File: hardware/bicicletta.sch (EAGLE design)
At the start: 21 parts, among them IC1 LM5017, IC2 LM1117-3.3

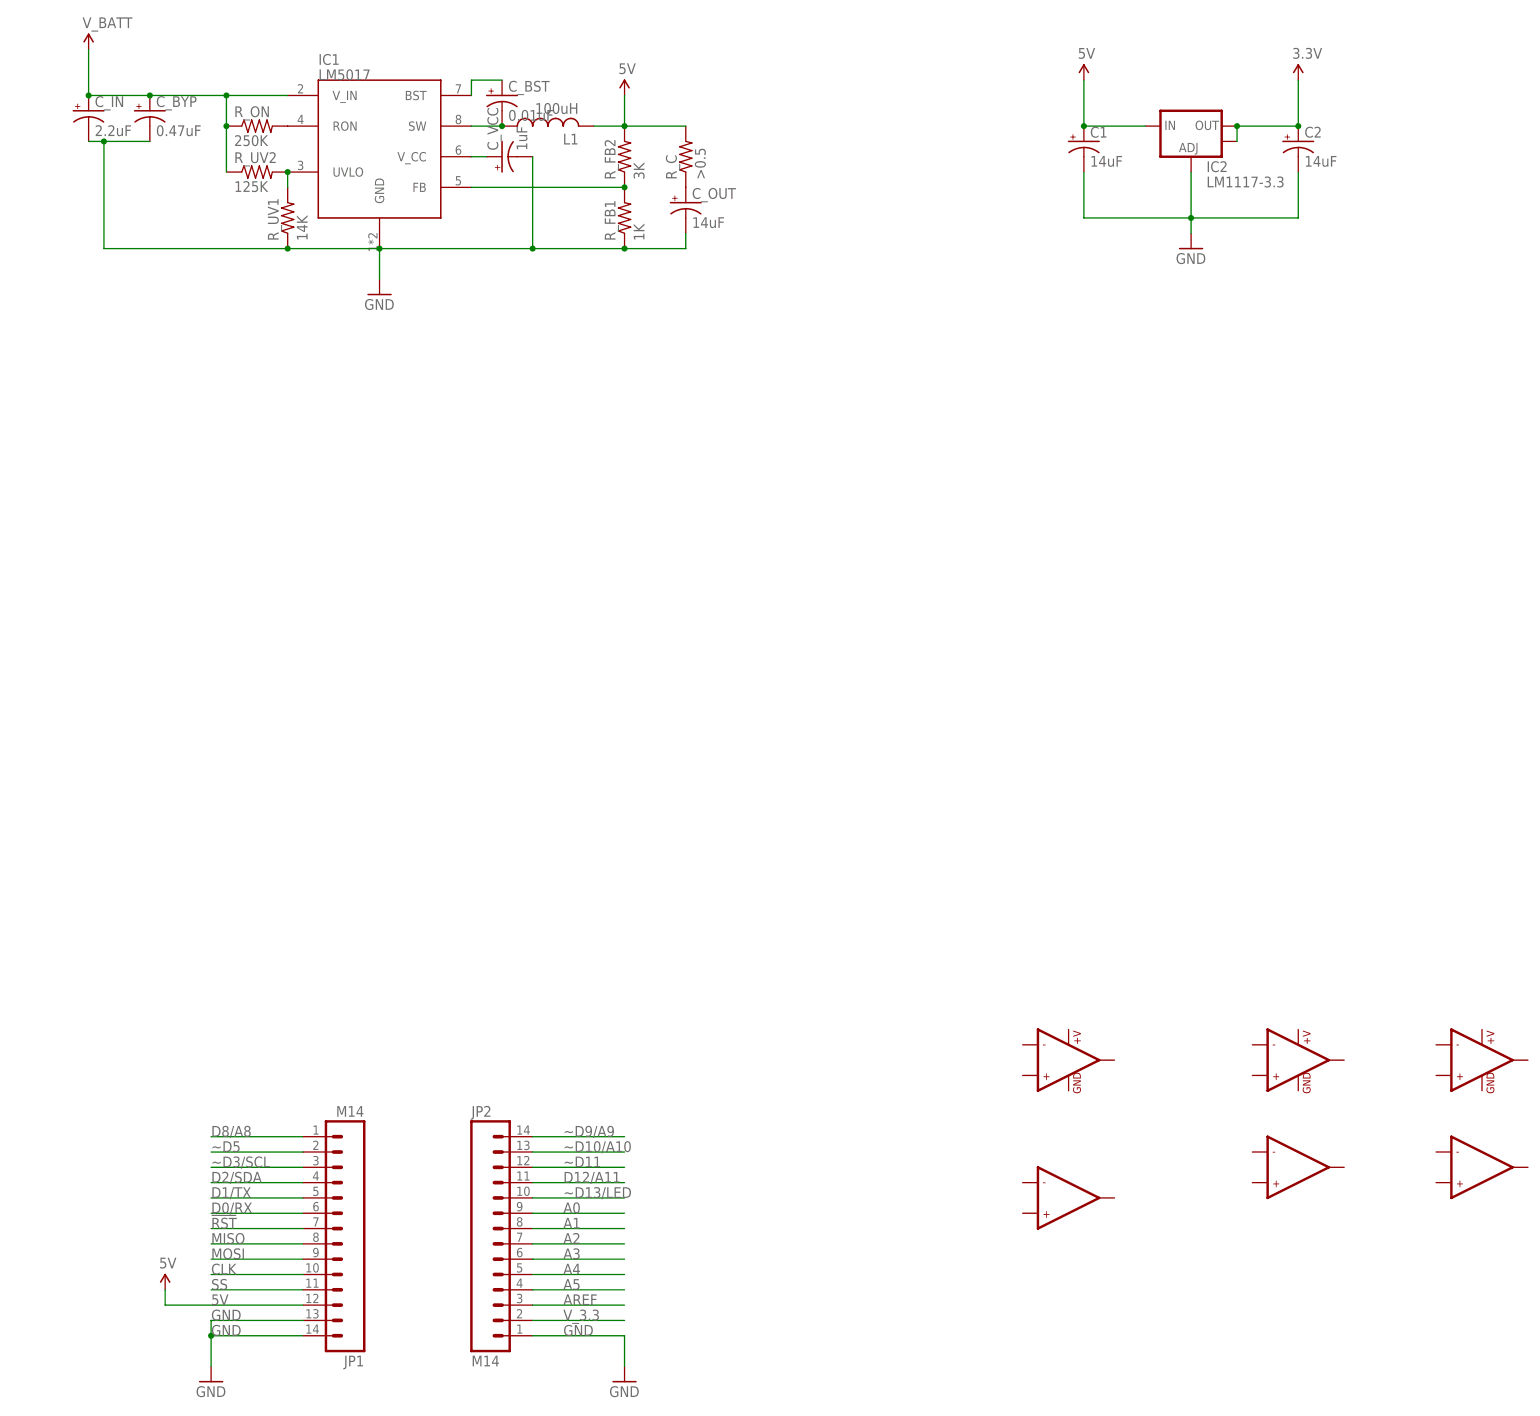
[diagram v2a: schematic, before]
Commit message: Added analog voltage shifter of dubious quality. WOrks in simulation
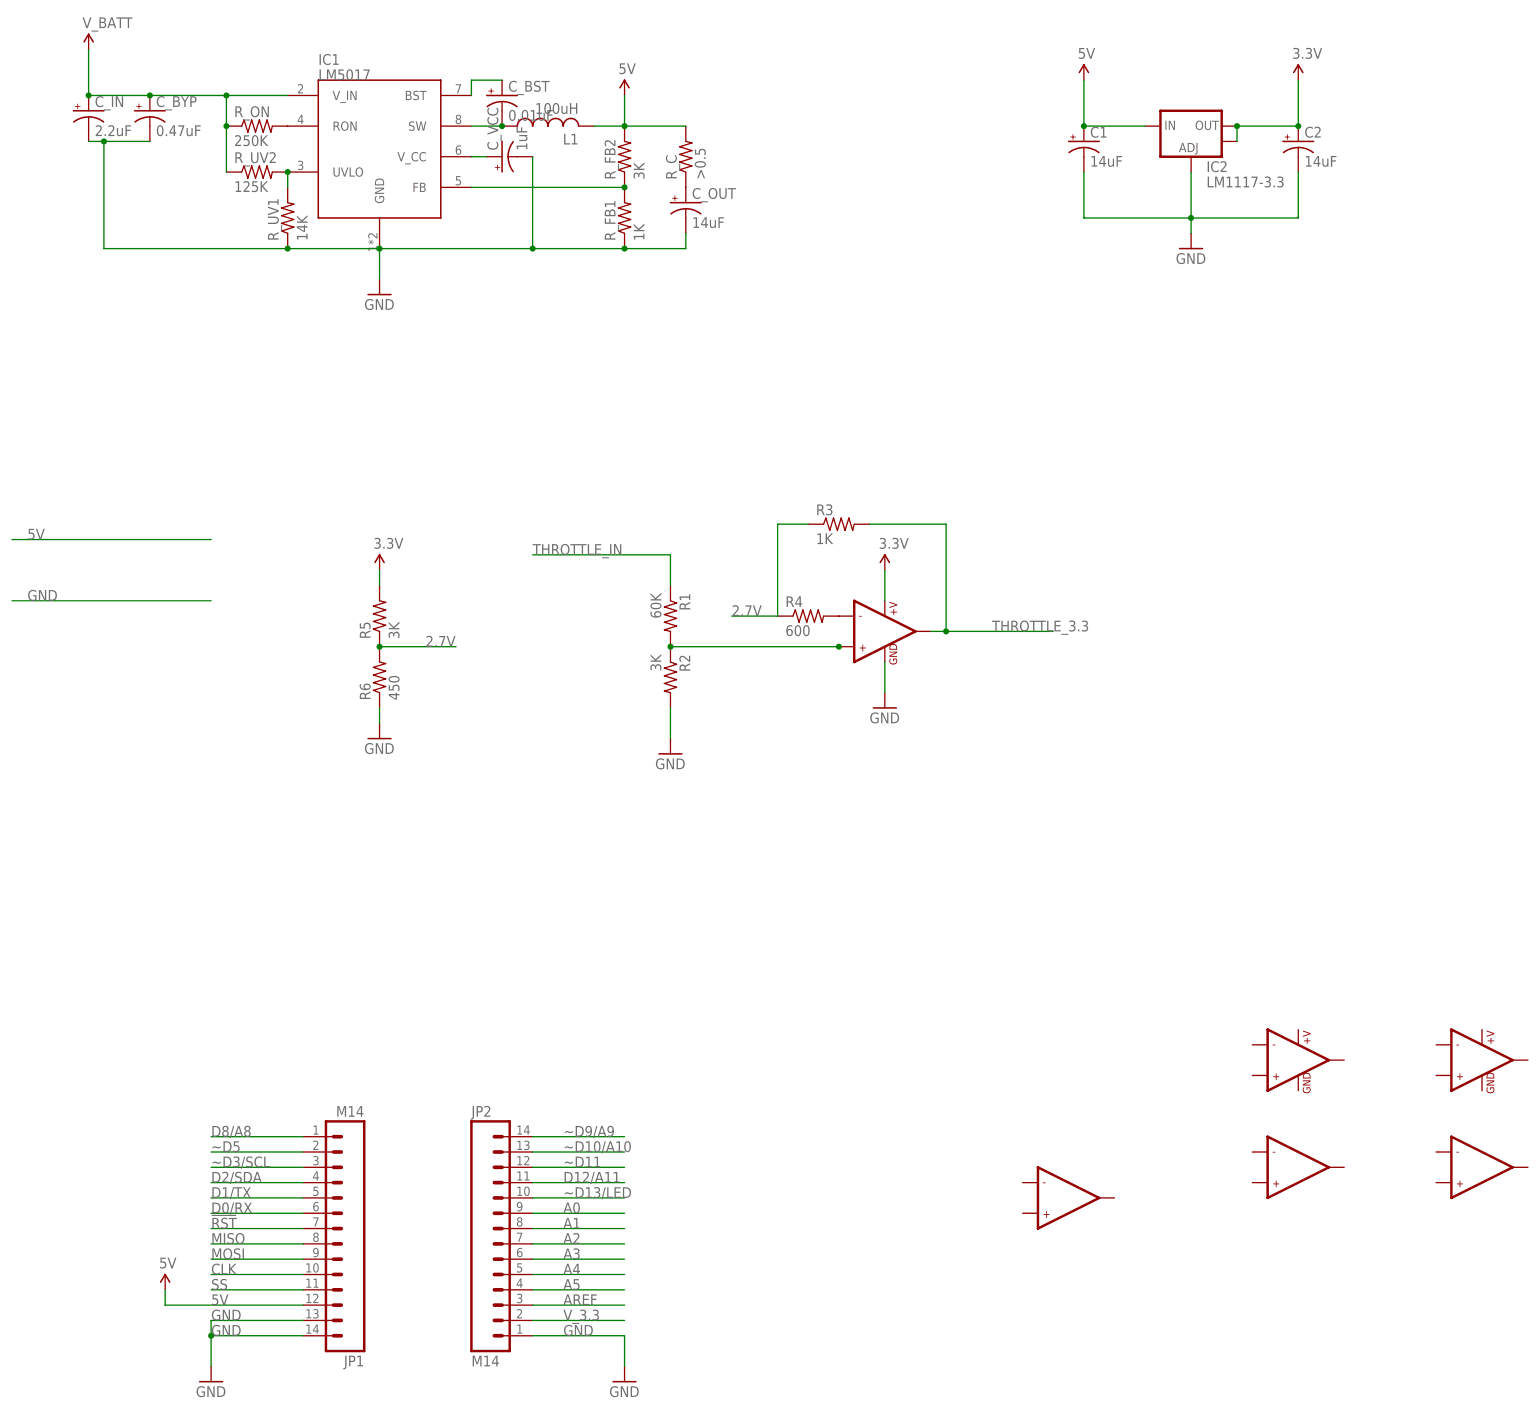
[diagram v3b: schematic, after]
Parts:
- added R1: 60K, rcl:R-US_M0805
- added R2, R5: 3K, rcl:R-US_M0805
- added R3: 1K, rcl:R-US_M0805
- added R4: 600, rcl:R-US_M0805
- added R6: 450, rcl:R-US_M0805
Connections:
- new net 2.7V: R3.1, R4.1, R5.1, R6.2
- new net N$10: R4.2, U$1G$1.-IN1
- new net N$8: R1.2, R2.1, U$1G$1.+IN1
- new net THROTTLE_3.3: R3.2, U$1G$1.OUT1
- new net THROTTLE_IN: R1.1
- net 3.3V: now also R5.2, U$1G$1.+V
- net GND: now also R2.2, R6.1, U$1G$1.GND
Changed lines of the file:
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@@
 <part name="C1" library="rcl" deviceset="CPOL-US" device="UD-5X5,8" value="14uF"/>
 <part name="C2" library="rcl" deviceset="CPOL-US" device="UD-5X5,8" value="14uF"/>
+<part name="R1" library="rcl" deviceset="R-US_" device="M0805" value="60K"/>
+<part name="R2" library="rcl" deviceset="R-US_" device="M0805" value="3K"/>
+<part name="GND5" library="SparkFun-Aesthetics" deviceset="GND" device=""/>
+<part name="R3" library="rcl" deviceset="R-US_" device="M0805" value="1K"/>
+<part name="R4" library="rcl" deviceset="R-US_" device="M0805" value="600"/>
+<part name="R5" library="rcl" deviceset="R-US_" device="M0805" value="3K"/>
+<part name="R6" library="rcl" deviceset="R-US_" device="M0805" value="450"/>
+<part name="GND6" library="SparkFun-Aesthetics" deviceset="GND" device=""/>
+<part name="P+2" library="SparkFun-Aesthetics" deviceset="3.3V" device=""/>
+<part name="P+3" library="SparkFun-Aesthetics" deviceset="3.3V" device=""/>
+<part name="GND7" library="SparkFun-Aesthetics" deviceset="GND" device=""/>
 </parts>
 <sheets>
@@
 <instance part="JP1" gate="G$1" x="53.34" y="53.34" rot="R180"/>
 <instance part="JP2" gate="G$1" x="71.12" y="55.88"/>
-<instance part="U$1" gate="G$1" x="170.18" y="83.82"/>
+<instance part="U$1" gate="G$1" x="139.7" y="154.94"/>
 <instance part="U$1" gate="G$2" x="170.18" y="60.96"/>
 <instance part="U$2" gate="G$1" x="208.28" y="83.82"/>
@@
 <instance part="C1" gate="G$1" x="172.72" y="236.22"/>
 <instance part="C2" gate="G$1" x="208.28" y="236.22"/>
+<instance part="R1" gate="G$1" x="104.14" y="157.48" rot="R270"/>
+<instance part="R2" gate="G$1" x="104.14" y="147.32" rot="R270"/>
+<instance part="GND5" gate="1" x="104.14" y="134.62"/>
+<instance part="R3" gate="G$1" x="132.08" y="172.72"/>
+<instance part="R4" gate="G$1" x="127" y="157.48"/>
+<instance part="R5" gate="G$1" x="55.88" y="157.48" rot="R90"/>
+<instance part="R6" gate="G$1" x="55.88" y="147.32" rot="R90"/>
+<instance part="GND6" gate="1" x="139.7" y="142.24"/>
+<instance part="P+2" gate="G$1" x="139.7" y="165.1"/>
+<instance part="P+3" gate="G$1" x="55.88" y="165.1"/>
+<instance part="GND7" gate="1" x="55.88" y="137.16"/>
 </instances>
 <busses>
@@
 <junction x="190.5" y="223.52"/>
 </segment>
+<segment>
+<wire x1="-5.08" y1="160.02" x2="27.94" y2="160.02" width="0.1524" layer="91"/>
+<label x="-2.54" y="160.02" size="1.778" layer="95"/>
+</segment>
+<segment>
+<pinref part="R2" gate="G$1" pin="2"/>
+<pinref part="GND5" gate="1" pin="GND"/>
+<wire x1="104.14" y1="137.16" x2="104.14" y2="142.24" width="0.1524" layer="91"/>
+</segment>
+<segment>
+<pinref part="U$1" gate="G$1" pin="GND"/>
+<pinref part="GND6" gate="1" pin="GND"/>
+<wire x1="139.7" y1="144.78" x2="139.7" y2="149.86" width="0.1524" layer="91"/>
+</segment>
+<segment>
+<pinref part="R6" gate="G$1" pin="1"/>
+<wire x1="55.88" y1="139.7" x2="55.88" y2="142.24" width="0.1524" layer="91"/>
+<pinref part="GND7" gate="1" pin="GND"/>
+</segment>
 </net>
 <net name="~D9/A9" class="0">
@@
 <junction x="172.72" y="238.76"/>
 </segment>
+<segment>
+<wire x1="-5.08" y1="170.18" x2="27.94" y2="170.18" width="0.1524" layer="91"/>
+<label x="-2.54" y="170.18" size="1.778" layer="95"/>
+</segment>
 </net>
 <net name="N$1" class="0">
@@
 <junction x="198.12" y="238.76"/>
 </segment>
-</net>
+<segment>
+<pinref part="U$1" gate="G$1" pin="+V"/>
+<pinref part="P+2" gate="G$1" pin="3.3V"/>
+<wire x1="139.7" y1="165.1" x2="139.7" y2="160.02" width="0.1524" layer="91"/>
+</segment>
+<segment>
+<pinref part="R5" gate="G$1" pin="2"/>
+<pinref part="P+3" gate="G$1" pin="3.3V"/>
+<wire x1="55.88" y1="165.1" x2="55.88" y2="162.56" width="0.1524" layer="91"/>
+</segment>
+</net>
+<net name="THROTTLE_IN" class="0">
+<segment>
+<wire x1="81.28" y1="167.64" x2="104.14" y2="167.64" width="0.1524" layer="91"/>
+<label x="81.28" y="167.64" size="1.778" layer="95"/>
+<pinref part="R1" gate="G$1" pin="1"/>
+<wire x1="104.14" y1="167.64" x2="104.14" y2="162.56" width="0.1524" layer="91"/>
+</segment>
+</net>
+<net name="N$8" class="0">
+<segment>
+<pinref part="R1" gate="G$1" pin="2"/>
+<pinref part="R2" gate="G$1" pin="1"/>
+<pinref part="U$1" gate="G$1" pin="+IN1"/>
+<junction x="132.08" y="152.4"/>
+<pinref part="U$1" gate="G$1" pin="+IN1"/>
+<wire x1="132.08" y1="152.4" x2="104.14" y2="152.4" width="0.1524" layer="91"/>
+<junction x="104.14" y="152.4"/>
+</segment>
+</net>
+<net name="THROTTLE_3.3" class="0">
+<segment>
+<pinref part="U$1" gate="G$1" pin="OUT1"/>
+<wire x1="147.32" y1="154.94" x2="149.86" y2="154.94" width="0.1524" layer="91"/>
+<label x="157.48" y="154.94" size="1.778" layer="95"/>
+<pinref part="R3" gate="G$1" pin="2"/>
+<wire x1="149.86" y1="154.94" x2="167.64" y2="154.94" width="0.1524" layer="91"/>
+<wire x1="137.16" y1="172.72" x2="149.86" y2="172.72" width="0.1524" layer="91"/>
+<wire x1="149.86" y1="172.72" x2="149.86" y2="154.94" width="0.1524" layer="91"/>
+<junction x="149.86" y="154.94"/>
+</segment>
+</net>
+<net name="N$10" class="0">
+<segment>
+<pinref part="R4" gate="G$1" pin="2"/>
+<pinref part="U$1" gate="G$1" pin="-IN1"/>
+</segment>
+</net>
+<net name="2.7V" class="0">
+<segment>
+<pinref part="R3" gate="G$1" pin="1"/>
+<pinref part="R4" gate="G$1" pin="1"/>
+<wire x1="127" y1="172.72" x2="121.92" y2="172.72" width="0.1524" layer="91"/>
+<wire x1="121.92" y1="172.72" x2="121.92" y2="157.48" width="0.1524" layer="91"/>
+<label x="114.3" y="157.48" size="1.778" layer="95"/>
+<wire x1="121.92" y1="157.48" x2="114.3" y2="157.48" width="0.1524" layer="91"/>
+</segment>
+<segment>
+<pinref part="R6" gate="G$1" pin="2"/>
+<pinref part="R5" gate="G$1" pin="1"/>
+<wire x1="55.88" y1="152.4" x2="68.58" y2="152.4" width="0.1524" layer="91"/>
+<junction x="55.88" y="152.4"/>
+<label x="63.5" y="152.4" size="1.778" layer="95"/>
+</segment>
+</net>

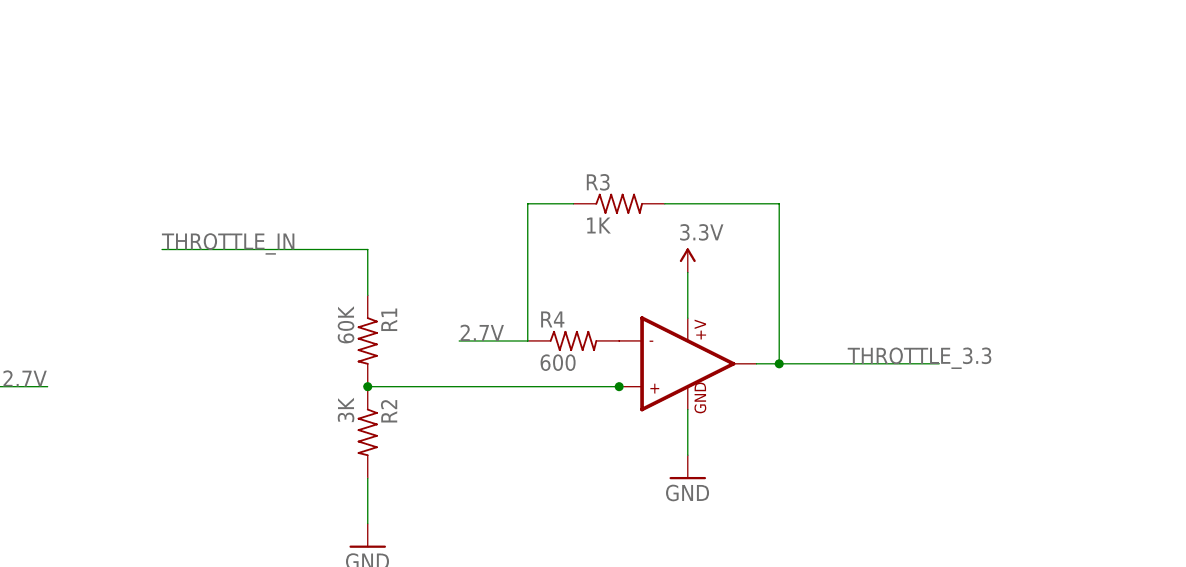
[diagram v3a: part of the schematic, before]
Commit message: Oh wait, this isn't for the throttle, this is for level-shifting the battery input. The input is scaled from 38-58V to 0-3.3V. Roughly.
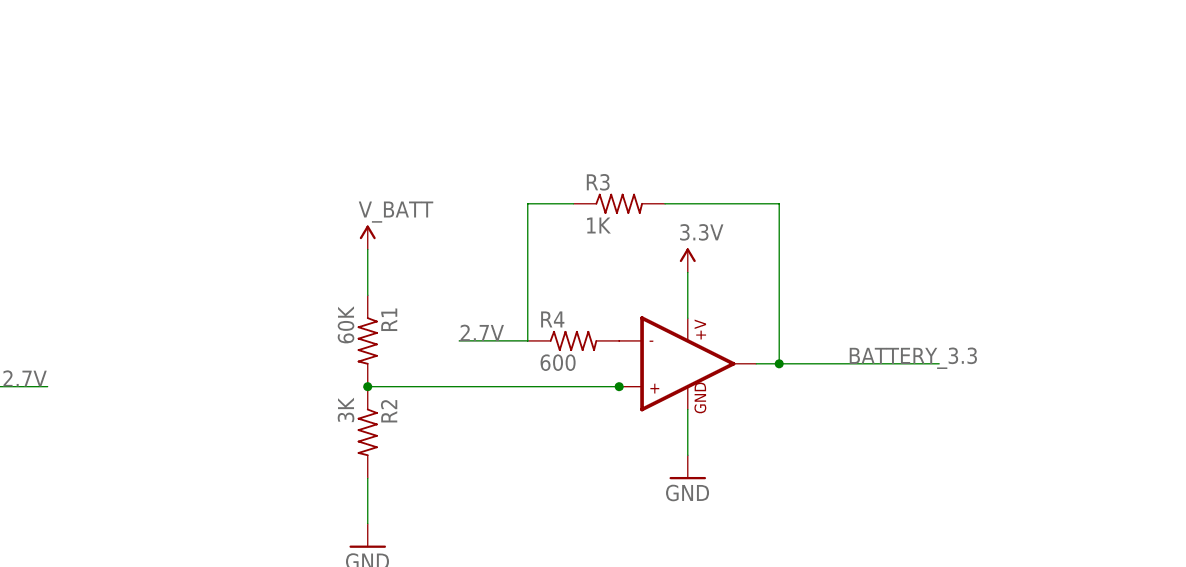
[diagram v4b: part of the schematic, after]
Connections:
- net THROTTLE_3.3 renamed BATTERY_3.3
- removed net 1.8V: C_BYP.+, C_IN.+, IC1.V_IN, R_ON.1, R_UV2.1
- removed net THROTTLE_IN: R1.1
- new net V_BATT: C_BYP.+, C_IN.+, IC1.V_IN, R1.1, R_ON.1, R_UV2.1
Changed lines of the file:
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@@
 <part name="P+3" library="SparkFun-Aesthetics" deviceset="3.3V" device=""/>
 <part name="GND7" library="SparkFun-Aesthetics" deviceset="GND" device=""/>
+<part name="U$4" library="SparkFun-Aesthetics" deviceset="V_BATT" device=""/>
 </parts>
 <sheets>
@@
 <instance part="P+3" gate="G$1" x="55.88" y="165.1"/>
 <instance part="GND7" gate="1" x="55.88" y="137.16"/>
+<instance part="U$4" gate="G$1" x="104.14" y="167.64"/>
 </instances>
 <busses>
@@
 </segment>
 </net>
-<net name="1.8V" class="0">
+<net name="V_BATT" class="0">
 <segment>
 <pinref part="U$6" gate="G$1" pin="1.8V"/>
@@
 <junction x="30.48" y="238.76"/>
 </segment>
+<segment>
+<pinref part="R1" gate="G$1" pin="1"/>
+<wire x1="104.14" y1="167.64" x2="104.14" y2="162.56" width="0.1524" layer="91"/>
+<pinref part="U$4" gate="G$1" pin="1.8V"/>
+</segment>
 </net>
 <net name="5V" class="0">
@@
 </segment>
 </net>
-<net name="THROTTLE_IN" class="0">
-<segment>
-<wire x1="81.28" y1="167.64" x2="104.14" y2="167.64" width="0.1524" layer="91"/>
-<label x="81.28" y="167.64" size="1.778" layer="95"/>
-<pinref part="R1" gate="G$1" pin="1"/>
-<wire x1="104.14" y1="167.64" x2="104.14" y2="162.56" width="0.1524" layer="91"/>
-</segment>
-</net>
 <net name="N$8" class="0">
 <segment>
@@
 </segment>
 </net>
-<net name="THROTTLE_3.3" class="0">
+<net name="BATTERY_3.3" class="0">
 <segment>
 <pinref part="U$1" gate="G$1" pin="OUT1"/>
